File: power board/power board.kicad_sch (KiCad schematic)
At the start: 22 parts, among them J1 Conn_02x02_ZigZag, J2 Conn_02x03_ZigZag, J3 Conn_02x02_ZigZag, J4 Conn_02x01, U1 YAAJ_DCDC_StepDown_LM2596, U3 XL6009

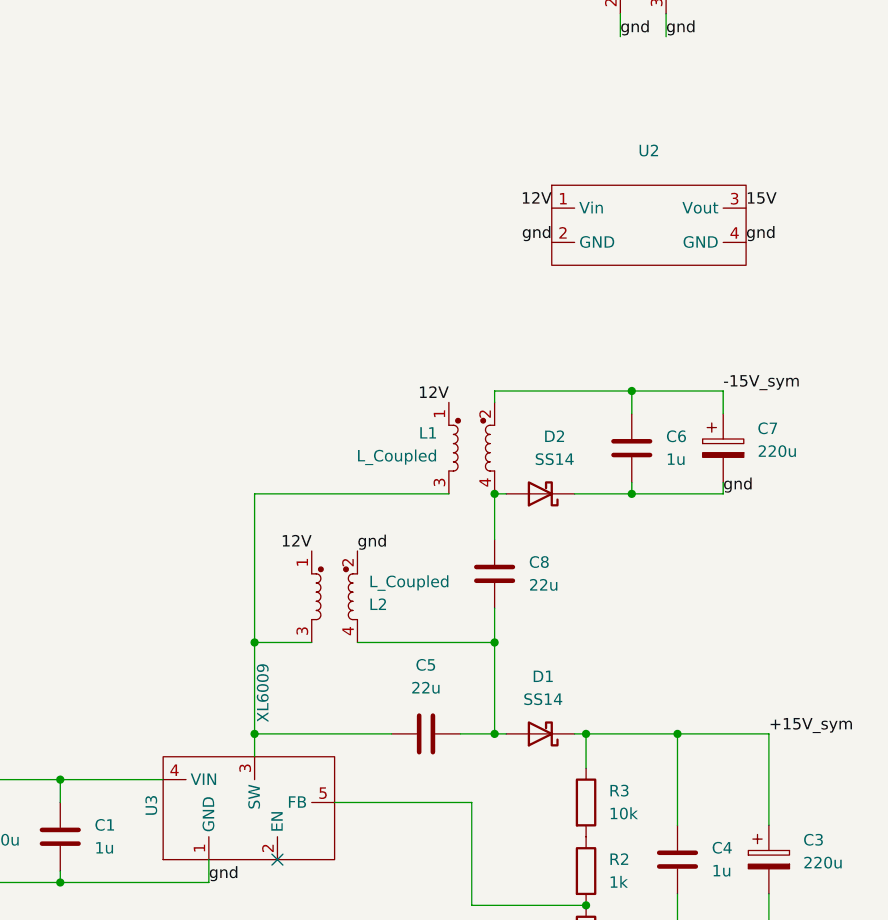
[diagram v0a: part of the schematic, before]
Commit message: Reorganização de pastas, udate da placa de alimentação
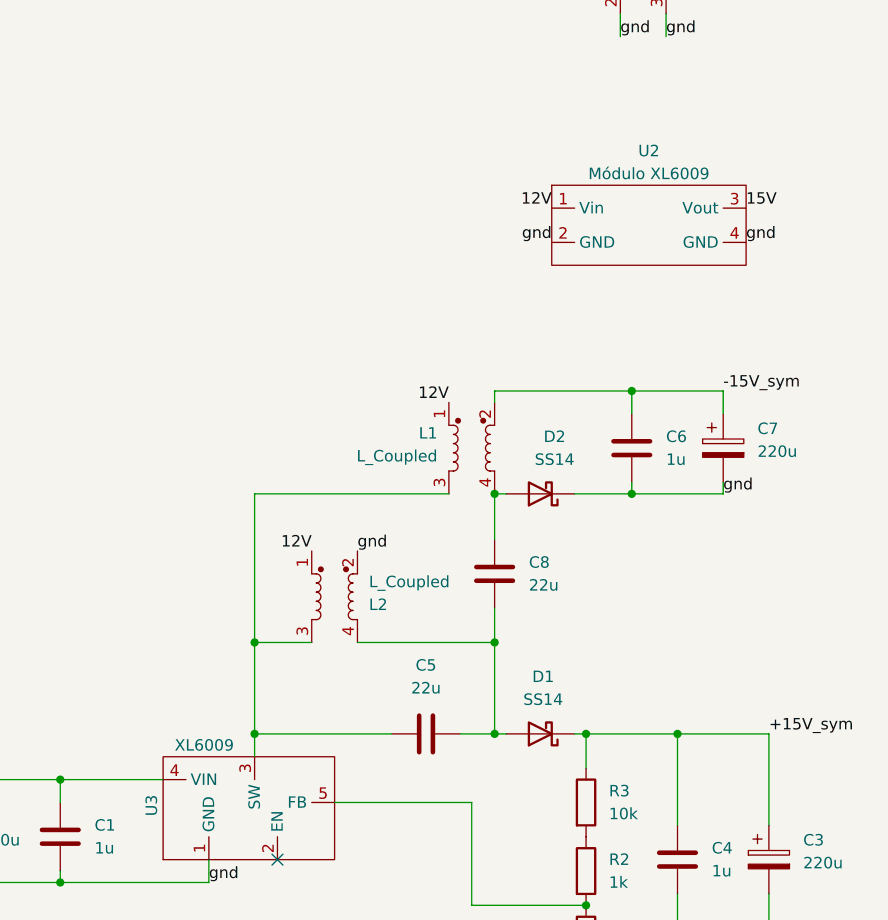
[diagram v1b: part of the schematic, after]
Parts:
- U2: value ~ -> Módulo XL6009
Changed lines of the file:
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@@
 		)
 		(property "Value" "XL6009"
-			(at 134.3025 124.46 0)
+			(at 131.064 127 90)
 			(effects
 				(font
@@
 			)
 		)
-		(property "Value" "~"
+		(property "Value" "Módulo XL6009"
 			(at 177.165 63.5 0)
 			(effects
